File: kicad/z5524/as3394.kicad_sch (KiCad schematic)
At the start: 36 parts, among them U11 DG442xY, U15 AS3394, U16 TL074

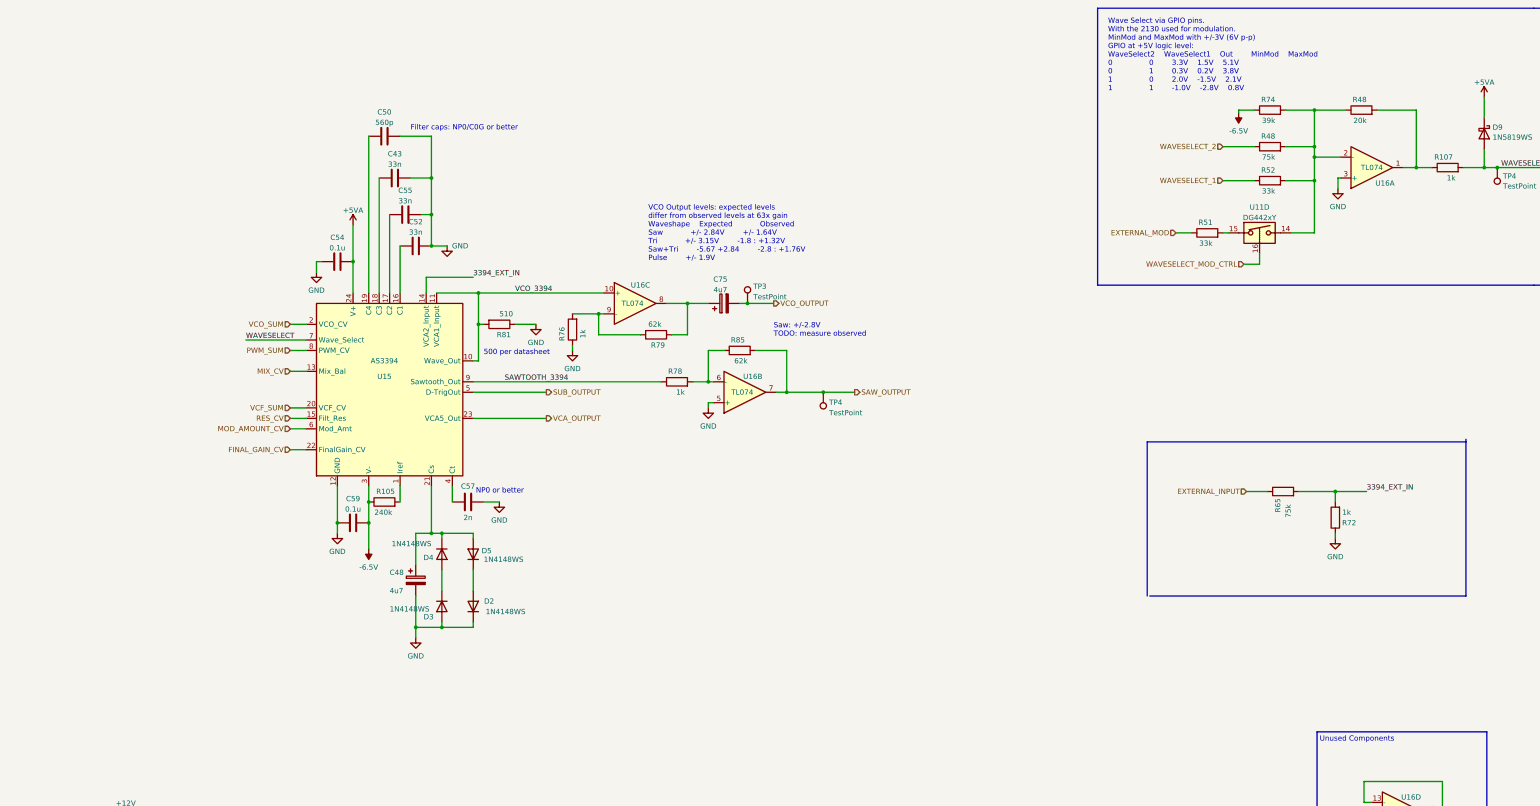
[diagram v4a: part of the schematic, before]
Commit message: updates to scale modulation values better
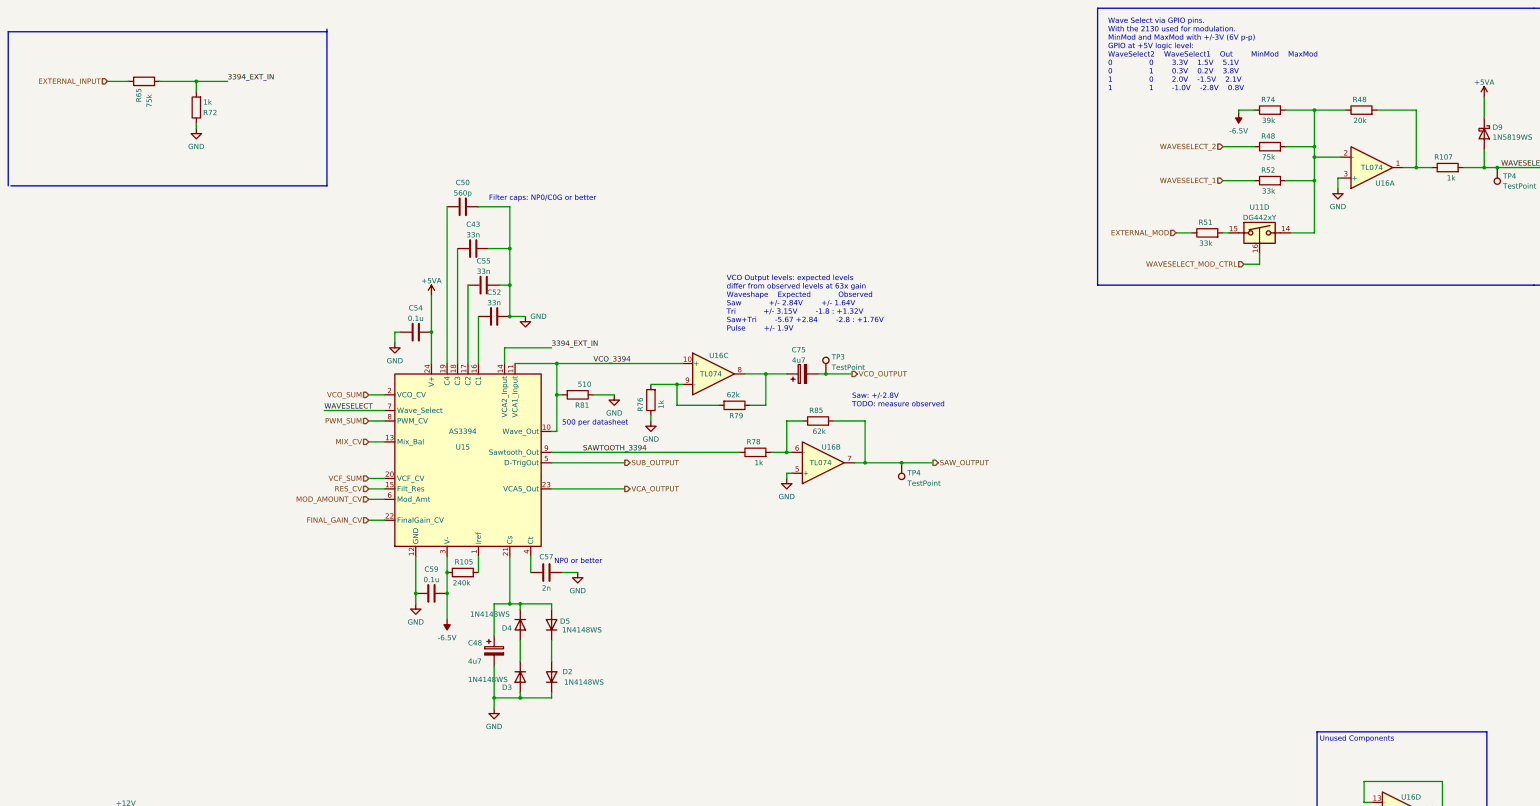
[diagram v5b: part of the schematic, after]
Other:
- moved on the sheet: C43, C48, C50, C52, C54, C55, C57, C59, C75, D2, D3, D4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

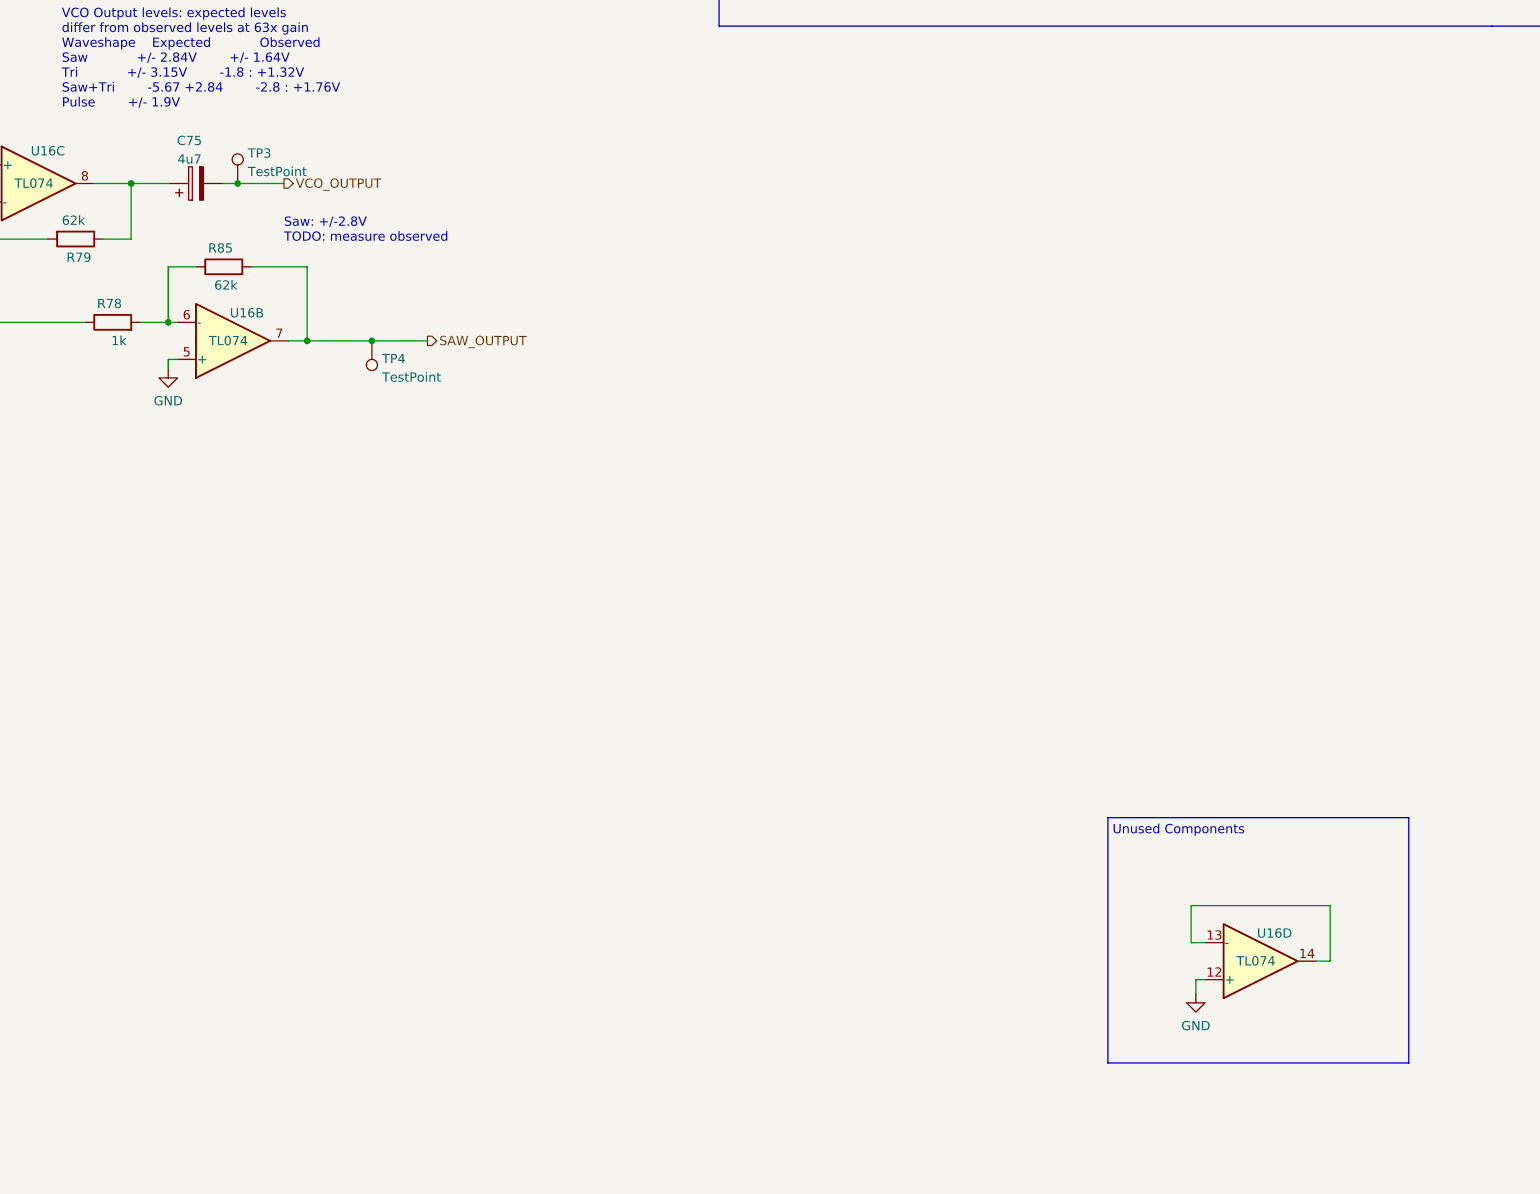
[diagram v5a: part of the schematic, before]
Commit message: schematic updates- cv values from dac and input protections between VCOs
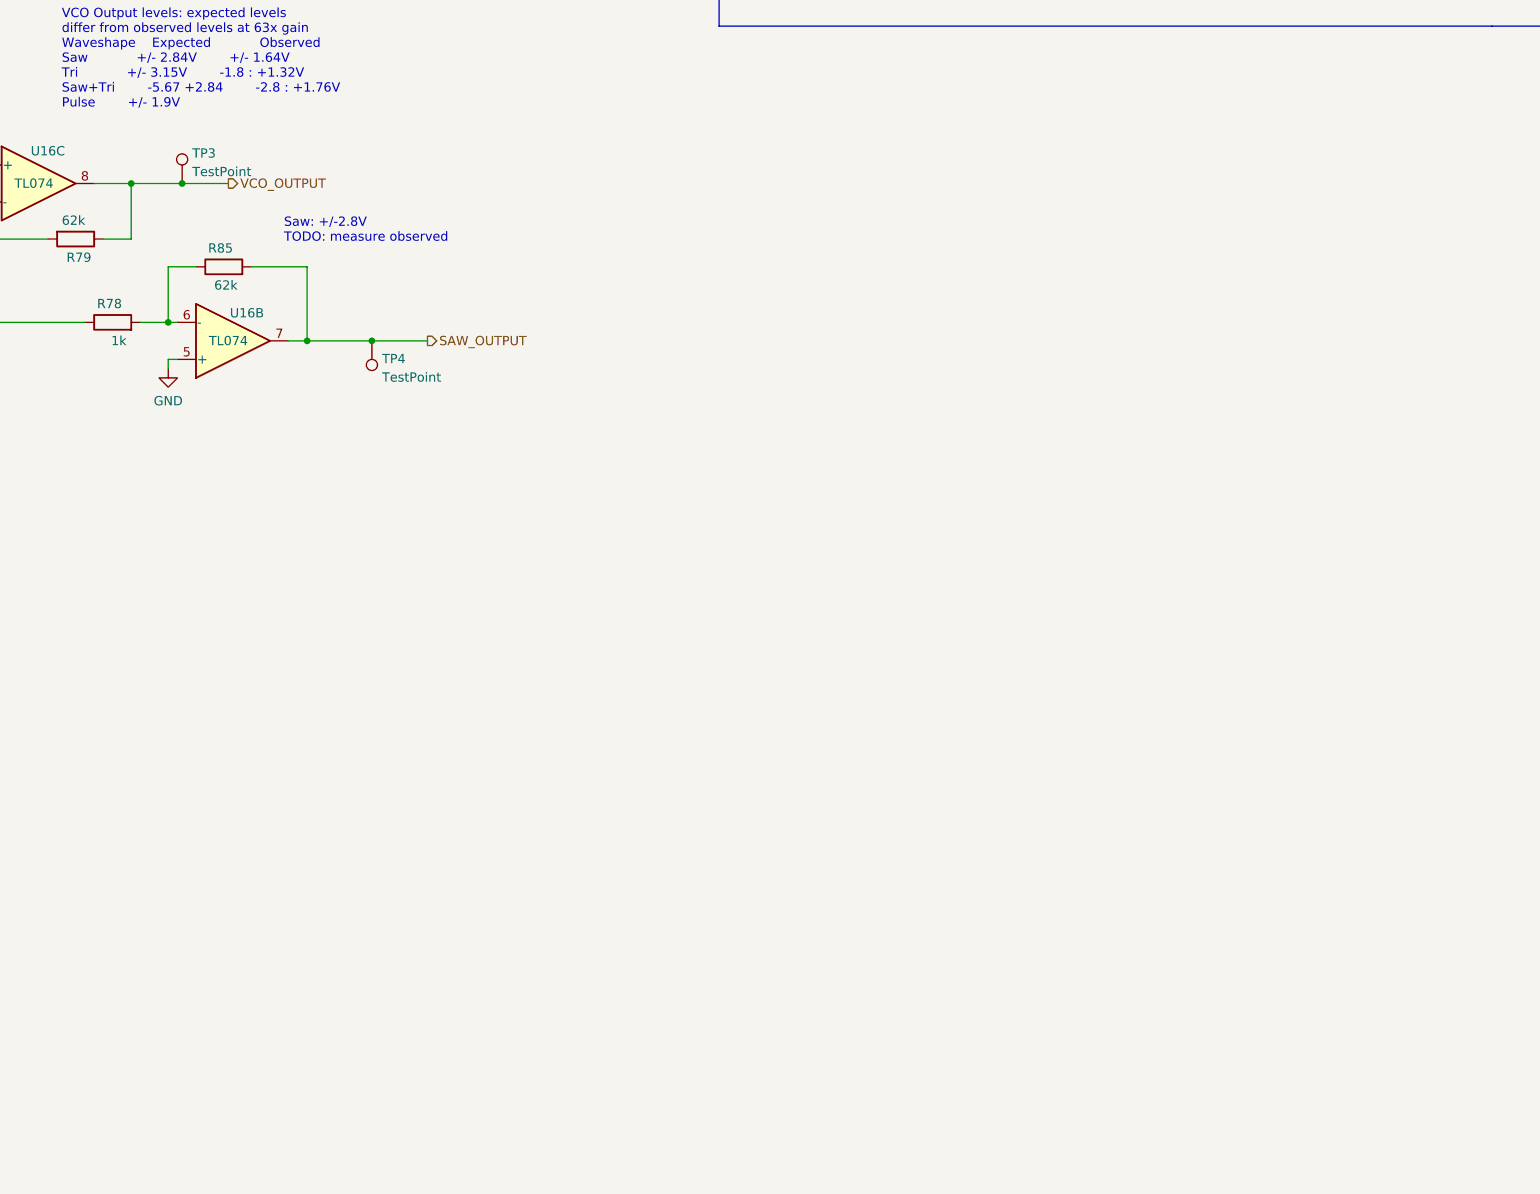
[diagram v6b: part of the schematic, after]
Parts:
- removed C75: 4u7, Capacitor_THT:CP_Radial_D4.0mm_P2.00mm, symbol Device:C_Polarized
- removed unit 4 of U16
- R48, R65: LCSC (none) -> C23242
- R51: LCSC (none) -> C4216
- R74: LCSC (none) -> C23153
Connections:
- net VCO_OUTPUT: now also R79.1, U16.8
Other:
- note removed: "Unused Components"
- moved on the sheet: TP3

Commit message: routed - initial at least
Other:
- title: Zoxnoxious SSI2130/AS3394 -> Zoxnoxious Z5524 (SSI2130/AS3394)
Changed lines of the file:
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@@
   (paper "B")
   (title_block
-    (title "Zoxnoxious SSI2130/AS3394")
-    (date "2023-08-27")
-    (rev "0.2")
+    (title "Zoxnoxious Z5524 (SSI2130/AS3394)")
+    (date "2023-12-06")
+    (rev "0.3")
     (company "Zoxnoxious Engineering")
   )

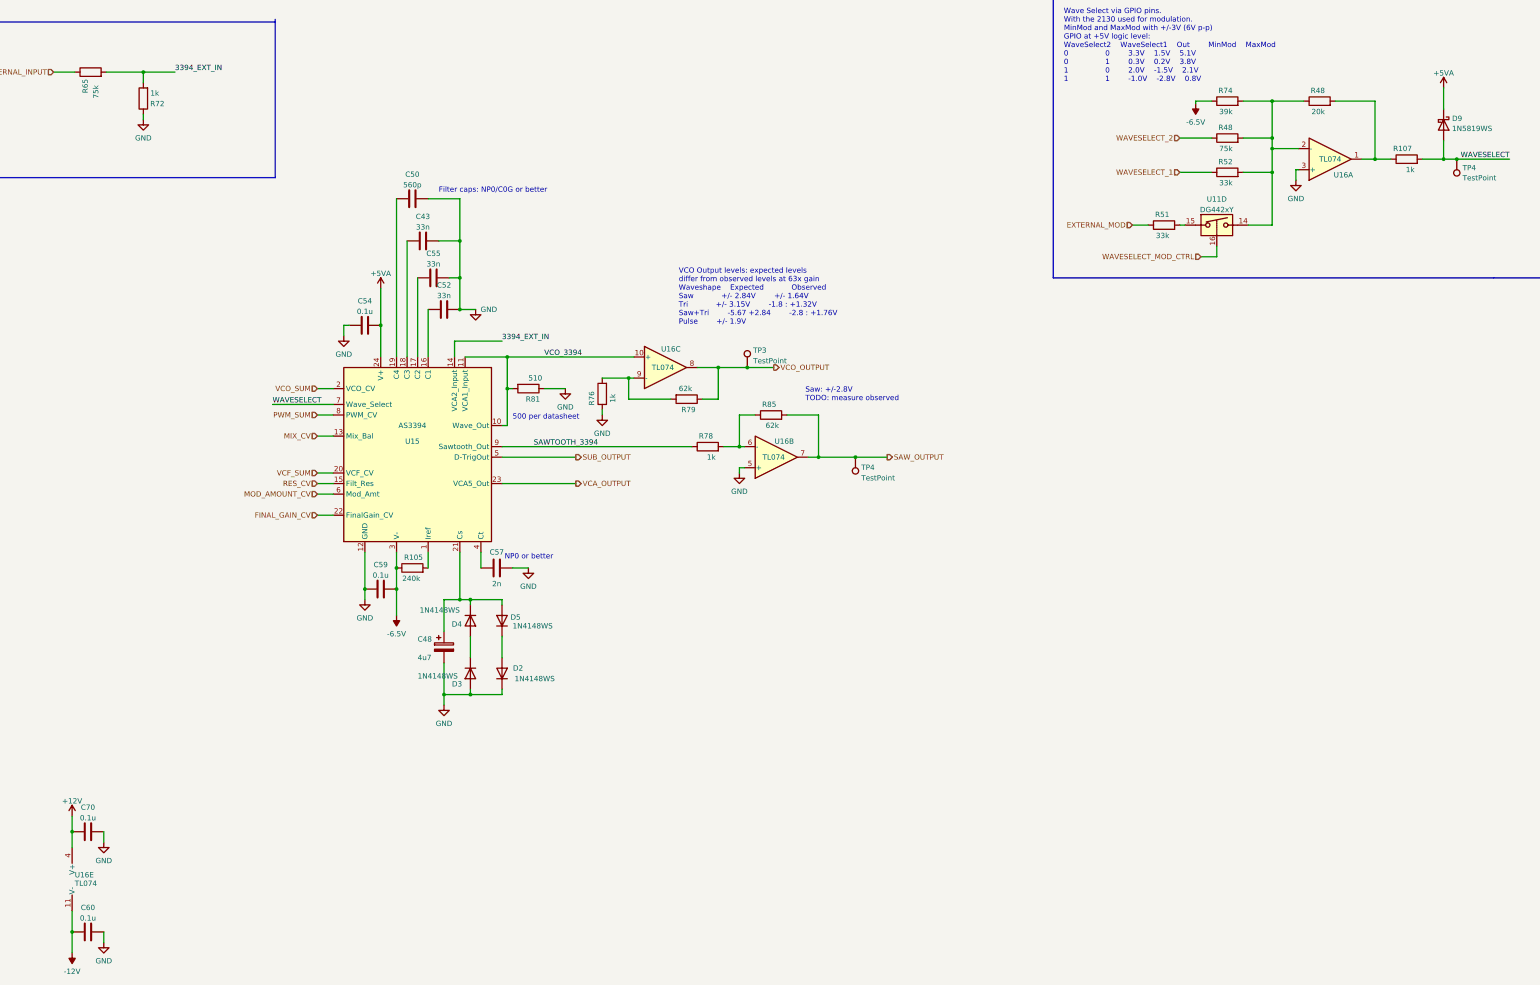
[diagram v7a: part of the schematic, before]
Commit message: getting silkscreen cleaned up
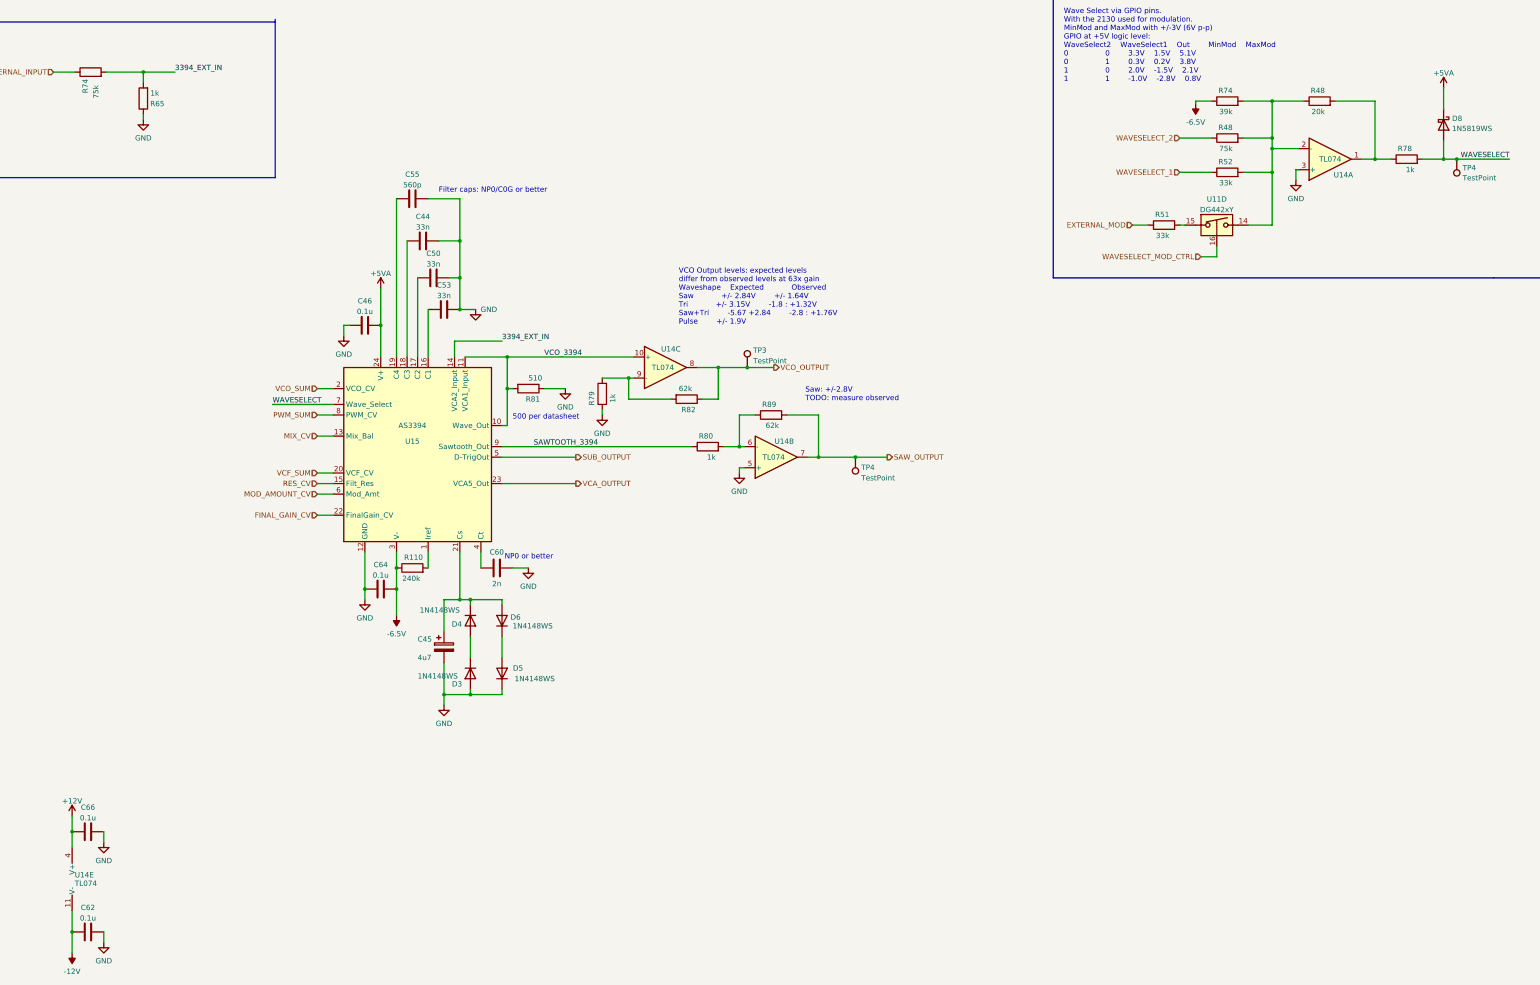
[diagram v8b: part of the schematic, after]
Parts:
- renumbered C43 to C44, C48 to C45, C54 to C46, C55 to C50, C52 to C53, C50 to C55, C57 to C60, C60 to C62, C59 to C64, C70 to C66, D2 to D5, D5 to D6, D9 to D8, R105 to R110, R72 to R65, R65 to R74, R107 to R78, R76 to R79, R78 to R80, R79 to R82, R85 to R89, U16 to U14
